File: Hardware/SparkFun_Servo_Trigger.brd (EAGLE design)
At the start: 22.9 x 43.2 mm, 30 parts, among them U1 ATTINY84, Y1 16MHZ

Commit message: Updates from checklist.
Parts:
- FRAME1: value (none) -> frame
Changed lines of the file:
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@@
 <layer number="19" name="Unrouted" color="6" fill="1" visible="yes" active="yes"/>
 <layer number="20" name="Dimension" color="15" fill="1" visible="yes" active="yes"/>
-<layer number="21" name="tPlace" color="16" fill="1" visible="no" active="yes"/>
+<layer number="21" name="tPlace" color="16" fill="1" visible="yes" active="yes"/>
 <layer number="22" name="bPlace" color="14" fill="1" visible="yes" active="yes"/>
 <layer number="23" name="tOrigins" color="15" fill="1" visible="yes" active="yes"/>
@@
 <layer number="27" name="tValues" color="7" fill="1" visible="no" active="yes"/>
 <layer number="28" name="bValues" color="7" fill="1" visible="no" active="yes"/>
-<layer number="29" name="tStop" color="7" fill="3" visible="no" active="yes"/>
+<layer number="29" name="tStop" color="7" fill="3" visible="yes" active="yes"/>
 <layer number="30" name="bStop" color="7" fill="6" visible="no" active="yes"/>
 <layer number="31" name="tCream" color="7" fill="4" visible="no" active="yes"/>
@@
 <layer number="37" name="tTest" color="7" fill="1" visible="no" active="yes"/>
 <layer number="38" name="bTest" color="7" fill="1" visible="no" active="yes"/>
-<layer number="39" name="tKeepout" color="4" fill="11" visible="no" active="yes"/>
-<layer number="40" name="bKeepout" color="1" fill="11" visible="no" active="yes"/>
+<layer number="39" name="tKeepout" color="4" fill="11" visible="yes" active="yes"/>
+<layer number="40" name="bKeepout" color="1" fill="11" visible="yes" active="yes"/>
 <layer number="41" name="tRestrict" color="4" fill="10" visible="no" active="yes"/>
 <layer number="42" name="bRestrict" color="1" fill="10" visible="no" active="yes"/>
@@
 <layer number="45" name="Holes" color="7" fill="1" visible="yes" active="yes"/>
 <layer number="46" name="Milling" color="3" fill="1" visible="no" active="yes"/>
-<layer number="47" name="Measures" color="7" fill="1" visible="no" active="yes"/>
+<layer number="47" name="Measures" color="7" fill="1" visible="yes" active="yes"/>
 <layer number="48" name="Document" color="7" fill="1" visible="no" active="yes"/>
 <layer number="49" name="Reference" color="7" fill="1" visible="no" active="yes"/>
@@
 </autorouter>
 <elements>
-<element name="FRAME1" library="SparkFun-Aesthetics" package="CREATIVE_COMMONS" value="" x="0" y="-19.05" smashed="yes">
+<element name="FRAME1" library="SparkFun-Aesthetics" package="CREATIVE_COMMONS" value="frame" x="0" y="-19.05" smashed="yes">
 <attribute name="VERSION" value="V11" x="8.255" y="0.635" size="1.27" layer="16" font="vector" ratio="20" rot="SMR0"/>
 <attribute name="DESIGNER" value="Byron Jacquot" x="30.48" y="-19.05" size="1.778" layer="51"/>

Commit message: Updating logos from library.
Using rounded-corner versions to save CAM time.
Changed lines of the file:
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@@
 <grid distance="0.05" unitdist="inch" unit="inch" style="lines" multiple="1" display="yes" altdistance="0.005" altunitdist="inch" altunit="inch"/>
 <layers>
-<layer number="1" name="Top" color="4" fill="1" visible="no" active="yes"/>
+<layer number="1" name="Top" color="4" fill="1" visible="yes" active="yes"/>
 <layer number="2" name="Route2" color="1" fill="3" visible="no" active="no"/>
 <layer number="3" name="Route3" color="4" fill="3" visible="no" active="no"/>
@@
 <layer number="14" name="Route14" color="1" fill="6" visible="no" active="no"/>
 <layer number="15" name="Route15" color="4" fill="6" visible="no" active="no"/>
-<layer number="16" name="Bottom" color="1" fill="1" visible="no" active="yes"/>
+<layer number="16" name="Bottom" color="1" fill="1" visible="yes" active="yes"/>
 <layer number="17" name="Pads" color="2" fill="1" visible="yes" active="yes"/>
 <layer number="18" name="Vias" color="2" fill="1" visible="yes" active="yes"/>
@@
 <layer number="27" name="tValues" color="7" fill="1" visible="no" active="yes"/>
 <layer number="28" name="bValues" color="7" fill="1" visible="no" active="yes"/>
-<layer number="29" name="tStop" color="7" fill="3" visible="yes" active="yes"/>
+<layer number="29" name="tStop" color="7" fill="3" visible="no" active="yes"/>
 <layer number="30" name="bStop" color="7" fill="6" visible="no" active="yes"/>
 <layer number="31" name="tCream" color="7" fill="4" visible="no" active="yes"/>
@@
 <layer number="37" name="tTest" color="7" fill="1" visible="no" active="yes"/>
 <layer number="38" name="bTest" color="7" fill="1" visible="no" active="yes"/>
-<layer number="39" name="tKeepout" color="4" fill="11" visible="yes" active="yes"/>
-<layer number="40" name="bKeepout" color="1" fill="11" visible="yes" active="yes"/>
+<layer number="39" name="tKeepout" color="4" fill="11" visible="no" active="yes"/>
+<layer number="40" name="bKeepout" color="1" fill="11" visible="no" active="yes"/>
 <layer number="41" name="tRestrict" color="4" fill="10" visible="no" active="yes"/>
 <layer number="42" name="bRestrict" color="1" fill="10" visible="no" active="yes"/>
@@
 <layer number="45" name="Holes" color="7" fill="1" visible="yes" active="yes"/>
 <layer number="46" name="Milling" color="3" fill="1" visible="no" active="yes"/>
-<layer number="47" name="Measures" color="7" fill="1" visible="yes" active="yes"/>
+<layer number="47" name="Measures" color="7" fill="1" visible="no" active="yes"/>
 <layer number="48" name="Document" color="7" fill="1" visible="no" active="yes"/>
 <layer number="49" name="Reference" color="7" fill="1" visible="no" active="yes"/>
@@
 <layer number="56" name="wert" color="7" fill="1" visible="no" active="no"/>
 <layer number="57" name="tCAD" color="7" fill="1" visible="no" active="no"/>
+<layer number="59" name="tCarbon" color="7" fill="1" visible="no" active="no"/>
+<layer number="60" name="bCarbon" color="7" fill="1" visible="no" active="no"/>
 <layer number="90" name="Modules" color="5" fill="1" visible="no" active="no"/>
 <layer number="91" name="Nets" color="2" fill="1" visible="no" active="no"/>
@@
 <layer number="112" name="tSilk" color="7" fill="1" visible="no" active="yes"/>
 <layer number="113" name="IDFDebug" color="4" fill="1" visible="no" active="yes"/>
+<layer number="114" name="Badge_Outline" color="7" fill="1" visible="yes" active="yes"/>
+<layer number="115" name="ReferenceISLANDS" color="7" fill="1" visible="yes" active="yes"/>
 <layer number="116" name="Patch_BOT" color="9" fill="4" visible="no" active="yes"/>
+<layer number="118" name="Rect_Pads" color="7" fill="1" visible="yes" active="yes"/>
 <layer number="121" name="_tsilk" color="7" fill="1" visible="no" active="yes"/>
 <layer number="122" name="_bsilk" color="7" fill="1" visible="no" active="yes"/>
@@
 <layer number="127" name="_tValues" color="7" fill="1" visible="no" active="yes"/>
 <layer number="128" name="_bValues" color="7" fill="1" visible="no" active="yes"/>
+<layer number="129" name="Mask" color="7" fill="1" visible="yes" active="yes"/>
 <layer number="131" name="tAdjust" color="7" fill="1" visible="no" active="yes"/>
 <layer number="132" name="bAdjust" color="7" fill="1" visible="no" active="yes"/>
@@
 <layer number="223" name="223bmp" color="24" fill="1" visible="no" active="no"/>
 <layer number="224" name="224bmp" color="25" fill="1" visible="no" active="no"/>
+<layer number="225" name="225bmp" color="7" fill="1" visible="yes" active="yes"/>
+<layer number="226" name="226bmp" color="7" fill="1" visible="yes" active="yes"/>
+<layer number="227" name="227bmp" color="7" fill="1" visible="yes" active="yes"/>
+<layer number="228" name="228bmp" color="7" fill="1" visible="yes" active="yes"/>
+<layer number="229" name="229bmp" color="7" fill="1" visible="yes" active="yes"/>
+<layer number="230" name="230bmp" color="7" fill="1" visible="yes" active="yes"/>
+<layer number="231" name="231bmp" color="7" fill="1" visible="yes" active="yes"/>
 <layer number="248" name="Housing" color="7" fill="1" visible="no" active="yes"/>
 <layer number="249" name="Edge" color="7" fill="1" visible="no" active="yes"/>
@@
 </autorouter>
 <elements>
-<element name="FRAME1" library="SparkFun-Aesthetics" package="CREATIVE_COMMONS" value="frame" x="0" y="-19.05" smashed="yes">
-<attribute name="VERSION" value="V11" x="8.255" y="0.635" size="1.27" layer="16" font="vector" ratio="20" rot="SMR0"/>
-<attribute name="DESIGNER" value="Byron Jacquot" x="30.48" y="-19.05" size="1.778" layer="51"/>
-</element>
+<element name="FRAME1" library="SparkFun-Aesthetics" package="CREATIVE_COMMONS" value="frame" x="0" y="-19.05" smashed="yes"/>
 <element name="R4" library="SparkFun-Resistors" package="0603-RES" value="10K" x="2.54" y="10.16" rot="R90">
 <attribute name="PROD_ID" value="RES-00824" x="2.54" y="10.16" size="1.778" layer="27" rot="R90" display="off"/>

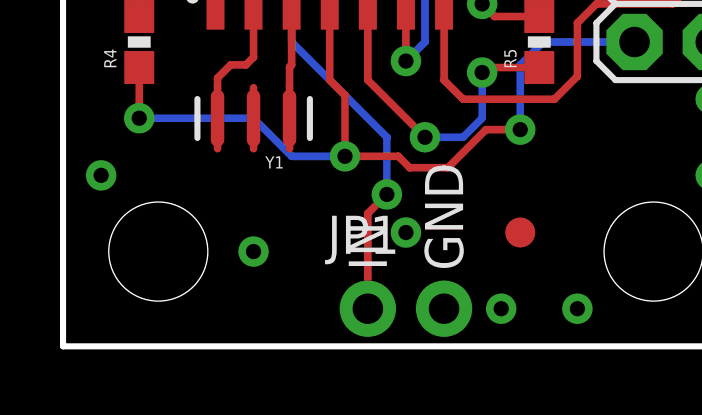
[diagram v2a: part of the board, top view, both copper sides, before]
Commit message: Replacing Designer name and version number.
They were part of the Frame, but it lost it's attributes in the library
update.
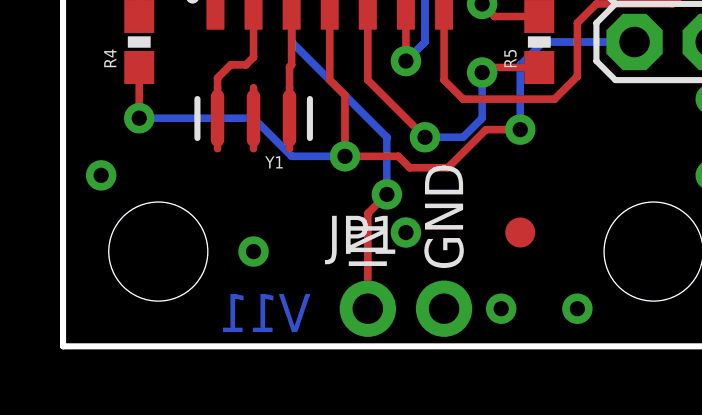
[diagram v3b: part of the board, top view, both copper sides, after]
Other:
- board text added: "Byron Jacquot"
- board text added: "V11"
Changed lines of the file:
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@@
 <layer number="112" name="tSilk" color="7" fill="1" visible="no" active="yes"/>
 <layer number="113" name="IDFDebug" color="4" fill="1" visible="no" active="yes"/>
-<layer number="114" name="Badge_Outline" color="7" fill="1" visible="yes" active="yes"/>
-<layer number="115" name="ReferenceISLANDS" color="7" fill="1" visible="yes" active="yes"/>
+<layer number="114" name="Badge_Outline" color="7" fill="1" visible="no" active="yes"/>
+<layer number="115" name="ReferenceISLANDS" color="7" fill="1" visible="no" active="yes"/>
 <layer number="116" name="Patch_BOT" color="9" fill="4" visible="no" active="yes"/>
-<layer number="118" name="Rect_Pads" color="7" fill="1" visible="yes" active="yes"/>
+<layer number="118" name="Rect_Pads" color="7" fill="1" visible="no" active="yes"/>
 <layer number="121" name="_tsilk" color="7" fill="1" visible="no" active="yes"/>
 <layer number="122" name="_bsilk" color="7" fill="1" visible="no" active="yes"/>
@@
 <layer number="127" name="_tValues" color="7" fill="1" visible="no" active="yes"/>
 <layer number="128" name="_bValues" color="7" fill="1" visible="no" active="yes"/>
-<layer number="129" name="Mask" color="7" fill="1" visible="yes" active="yes"/>
+<layer number="129" name="Mask" color="7" fill="1" visible="no" active="yes"/>
 <layer number="131" name="tAdjust" color="7" fill="1" visible="no" active="yes"/>
 <layer number="132" name="bAdjust" color="7" fill="1" visible="no" active="yes"/>
@@
 <layer number="223" name="223bmp" color="24" fill="1" visible="no" active="no"/>
 <layer number="224" name="224bmp" color="25" fill="1" visible="no" active="no"/>
-<layer number="225" name="225bmp" color="7" fill="1" visible="yes" active="yes"/>
-<layer number="226" name="226bmp" color="7" fill="1" visible="yes" active="yes"/>
-<layer number="227" name="227bmp" color="7" fill="1" visible="yes" active="yes"/>
-<layer number="228" name="228bmp" color="7" fill="1" visible="yes" active="yes"/>
-<layer number="229" name="229bmp" color="7" fill="1" visible="yes" active="yes"/>
-<layer number="230" name="230bmp" color="7" fill="1" visible="yes" active="yes"/>
-<layer number="231" name="231bmp" color="7" fill="1" visible="yes" active="yes"/>
+<layer number="225" name="225bmp" color="7" fill="1" visible="no" active="yes"/>
+<layer number="226" name="226bmp" color="7" fill="1" visible="no" active="yes"/>
+<layer number="227" name="227bmp" color="7" fill="1" visible="no" active="yes"/>
+<layer number="228" name="228bmp" color="7" fill="1" visible="no" active="yes"/>
+<layer number="229" name="229bmp" color="7" fill="1" visible="no" active="yes"/>
+<layer number="230" name="230bmp" color="7" fill="1" visible="no" active="yes"/>
+<layer number="231" name="231bmp" color="7" fill="1" visible="no" active="yes"/>
 <layer number="248" name="Housing" color="7" fill="1" visible="no" active="yes"/>
 <layer number="249" name="Edge" color="7" fill="1" visible="no" active="yes"/>
@@
 <rectangle x1="8.509" y1="30.607" x2="9.525" y2="31.623" layer="22"/>
 <wire x1="17.5" y1="15.9" x2="17.5" y2="14.6" width="0.254" layer="22"/>
+<text x="8.254" y="0.492" size="1.27" layer="16" font="vector" ratio="15" rot="MR0">V11</text>
+<text x="30.48" y="-19.05" size="1.778" layer="51" font="vector" ratio="10">Byron Jacquot</text>
 </plain>
 <attributes>
